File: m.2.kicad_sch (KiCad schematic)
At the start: 3 parts, among them J9 Bus_M.2_Socket_B

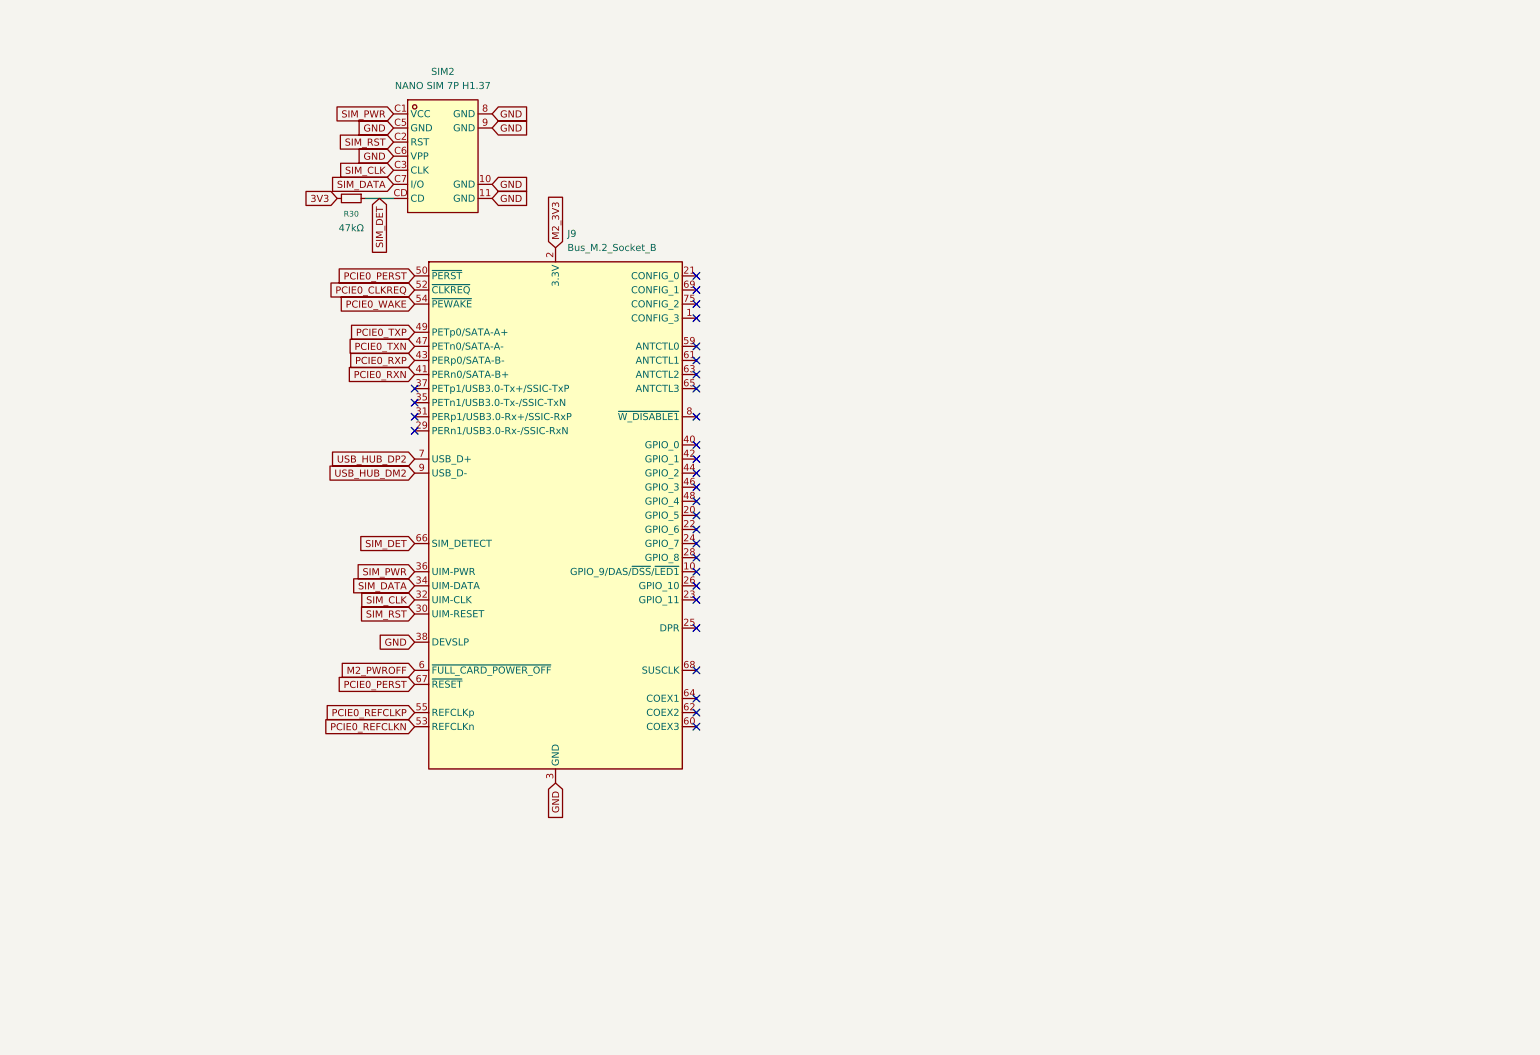
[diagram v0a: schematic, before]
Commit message: Move Data USB-C Port to IO + Add USB1 SS mux and SBU orientation switch, resolve CM5 GPIO assignments
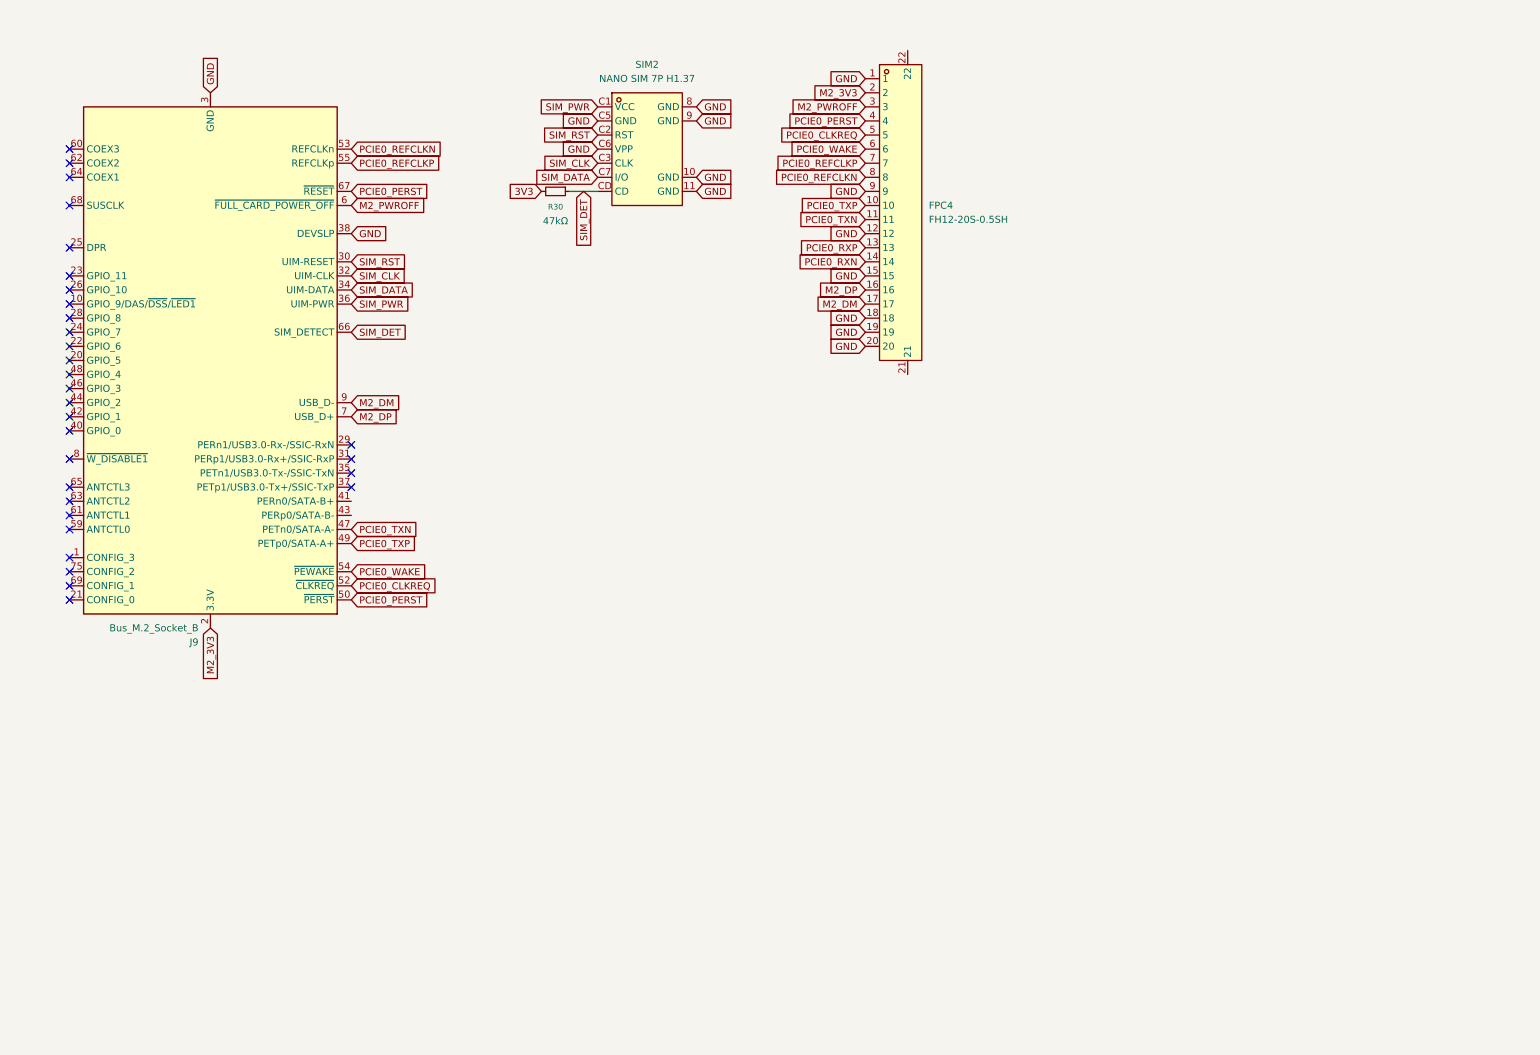
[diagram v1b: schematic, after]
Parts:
- added FPC4: FH12-20S-0.5SH, slate113:FPC-SMD_FH12-20S-0.5SH-55, symbol slate113:FH12-20S-0.5SH
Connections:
- net GND: now also FPC4.1, FPC4.12, FPC4.15, FPC4.18, FPC4.19, FPC4.20, FPC4.9
- net M2_3V3: now also FPC4.2
- net M2_PWROFF: now also FPC4.3
- net PCIE0_CLKREQ: now also FPC4.5
- net PCIE0_PERST: now also FPC4.4
- net PCIE0_REFCLKN: now also FPC4.8
- net PCIE0_REFCLKP: now also FPC4.7
- net PCIE0_RXN: now also FPC4.14; no longer J9.41 (PERn0/SATA-B+)
- net PCIE0_RXP: now also FPC4.13; no longer J9.43 (PERp0/SATA-B-)
- net PCIE0_TXN: now also FPC4.11
- net PCIE0_TXP: now also FPC4.10
- net PCIE0_WAKE: now also FPC4.6
- net USB_HUB_DM2 renamed M2_DM
- net M2_DM: now also FPC4.17
- net USB_HUB_DP2 renamed M2_DP
- net M2_DP: now also FPC4.16
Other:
- moved on the sheet: J9, R30, SIM2

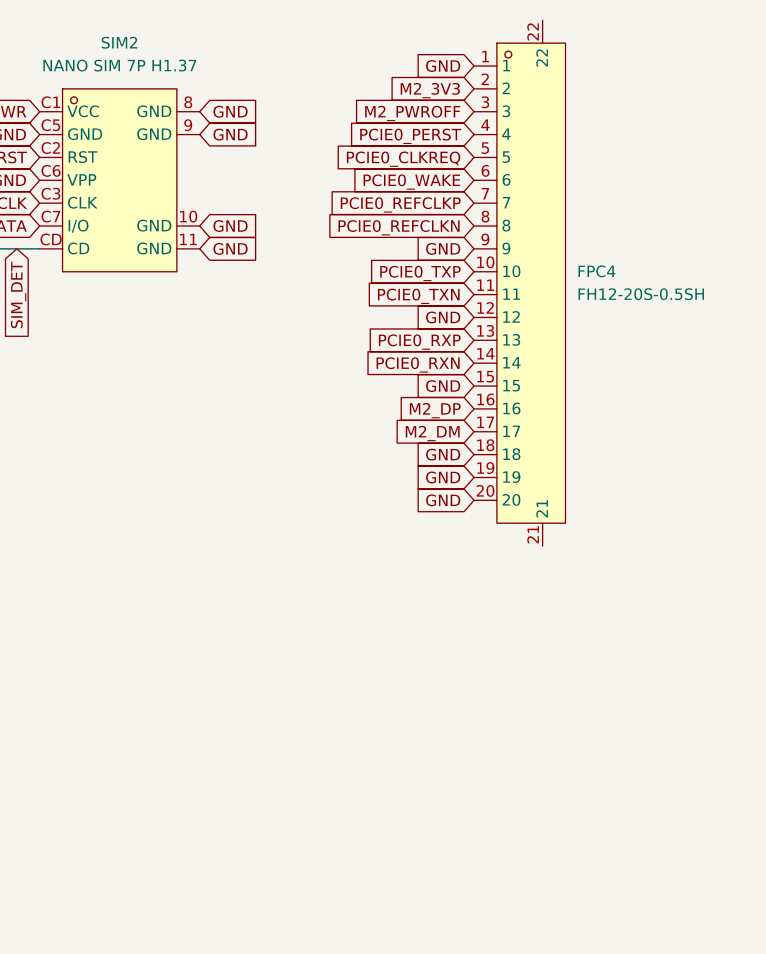
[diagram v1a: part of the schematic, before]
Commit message: add wifi+ble combo symbol, fix connector pin counts, slim b2b connectors, drop 3-way flex cable
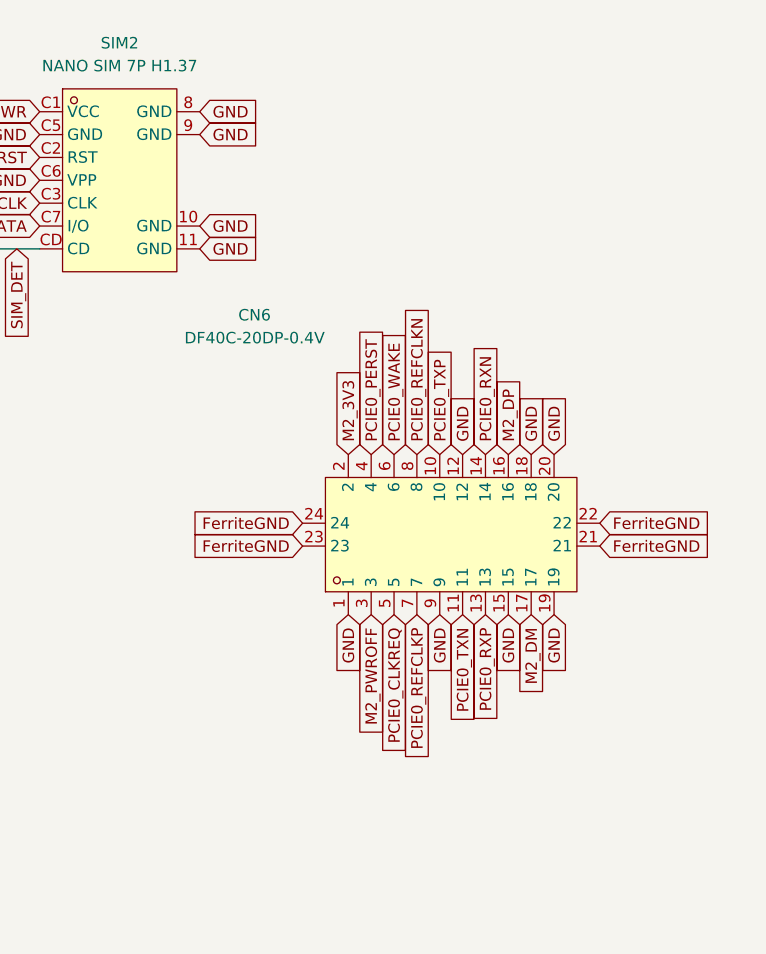
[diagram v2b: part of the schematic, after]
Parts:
- removed FPC4: FH12-20S-0.5SH, slate113:FPC-SMD_FH12-20S-0.5SH-55, symbol slate113:FH12-20S-0.5SH
- added CN6: DF40C-20DP-0.4V, slate113:CONN-SMD_20P-P0.40_HRS_DF40TC-20DP-0.4V, symbol slate113:DF40C-20DP-0.4V
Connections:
- net GND: now also CN6.1, CN6.12, CN6.15, CN6.18, CN6.19, CN6.20, CN6.9
- net M2_3V3: now also CN6.2
- net M2_DM: now also CN6.17
- net M2_DP: now also CN6.16
- net M2_PWROFF: now also CN6.3
- net PCIE0_CLKREQ: now also CN6.5
- net PCIE0_PERST: now also CN6.4
- net PCIE0_REFCLKN: now also CN6.8
- net PCIE0_REFCLKP: now also CN6.7
- net PCIE0_RXN: now also CN6.14
- net PCIE0_RXP: now also CN6.13
- net PCIE0_TXN: now also CN6.11
- net PCIE0_TXP: now also CN6.10
- net PCIE0_WAKE: now also CN6.6
- new net FerriteGND: CN6.21, CN6.22, CN6.23, CN6.24

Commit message: forgot to save
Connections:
- no-connect marks 30 -> 32
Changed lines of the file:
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@@
 	(generator_version "10.0")
 	(paper "A5")
+	(rectangle
+		(start 151.765 13.335)
+		(end 196.85 40.005)
+		(stroke
+			(width 0)
+			(type default)
+		)
+		(fill
+			(type none)
+		)
+	)
 	(no_connect
 		(at 20.32 63.5)
@@
 	)
 	(no_connect
+		(at 71.12 101.6)
+	)
+	(no_connect
 		(at 20.32 86.36)
 	)
@@
 	(no_connect
 		(at 20.32 104.14)
+	)
+	(no_connect
+		(at 71.12 99.06)
 	)
 	(no_connect
@@
 		(property "Intersheetrefs" "${INTERSHEET_REFS}"
 			(at 82.3299 63.5 0)
+			(hide yes)
+			(show_name no)
+			(do_not_autoplace no)
+			(effects
+				(font
+					(size 1.27 1.27)
+				)
+				(justify left)
+			)
+		)
+	)
+	(global_label "M2_3V3"
+		(shape input)
+		(at 194.31 24.13 90)
+		(fields_autoplaced yes)
+		(effects
+			(font
+				(size 1.27 1.27)
+			)
+			(justify left)
+		)
+		(property "Intersheetrefs" "${INTERSHEET_REFS}"
+			(at 194.31 14.0087 90)
 			(hide yes)
 			(show_name no)
@@
 					(unit 1)
 				)
+			)
+		)
+	)
+	(symbol
+		(lib_id "power:PWR_FLAG")
+		(at 194.31 24.13 180)
+		(unit 1)
+		(body_style 1)
+		(exclude_from_sim no)
+		(in_bom yes)
+		(on_board yes)
+		(in_pos_files yes)
+		(dnp no)
+		(property "Reference" "#FLG07"
+			(at 194.31 26.035 0)
+			(hide yes)
+			(show_name no)
+			(do_not_autoplace no)
+			(effects
+				(font
+					(size 1.27 1.27)
+				)
+			)
+		)
+		(property "Value" "PWR_FLAG"
+			(at 196.088 28.194 0)
+			(hide yes)
+			(show_name no)
+			(do_not_autoplace no)
+			(effects
+				(font
+					(size 1.27 1.27)
+				)
+			)
+		)
+		(property "Footprint" ""
+			(at 194.31 24.13 0)
+			(hide yes)
+			(show_name no)
+			(do_not_autoplace no)
+			(effects
+				(font
+					(size 1.27 1.27)
+				)
+			)
+		)
+		(property "Datasheet" ""
+			(at 194.31 24.13 0)
+			(hide yes)
+			(show_name no)
+			(do_not_autoplace no)
+			(effects
+				(font
+					(size 1.27 1.27)
+				)
+			)
+		)
+		(property "Description" "Special symbol for telling ERC where power comes from"
+			(at 194.31 24.13 0)
+			(hide yes)
+			(show_name no)
+			(do_not_autoplace no)
+			(effects
+				(font
+					(size 1.27 1.27)
+				)
+			)
+		)
+		(pin "1"
+		)
+		(instances
+			(project "slate113"
+				(path "/94414cfb-47f8-4293-934c-b1b4e6e41e9f"
+					(reference "#FLG07")
+					(unit 1)
+				)

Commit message: finished gps schematic, updated footprints and 3d models
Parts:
- J9: footprint (none) -> slate113:NGFFM_2BKEY_8_2_COPY
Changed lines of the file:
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@@
 			)
 		)
-		(property "Footprint" ""
+		(property "Footprint" "slate113:NGFFM_2BKEY_8_2_COPY"
 			(at 45.72 100.33 0)
 			(hide yes)
